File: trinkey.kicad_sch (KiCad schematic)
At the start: 7 parts, among them J1 USB_A, U1 RP2040, U2 AMS1117-3.3

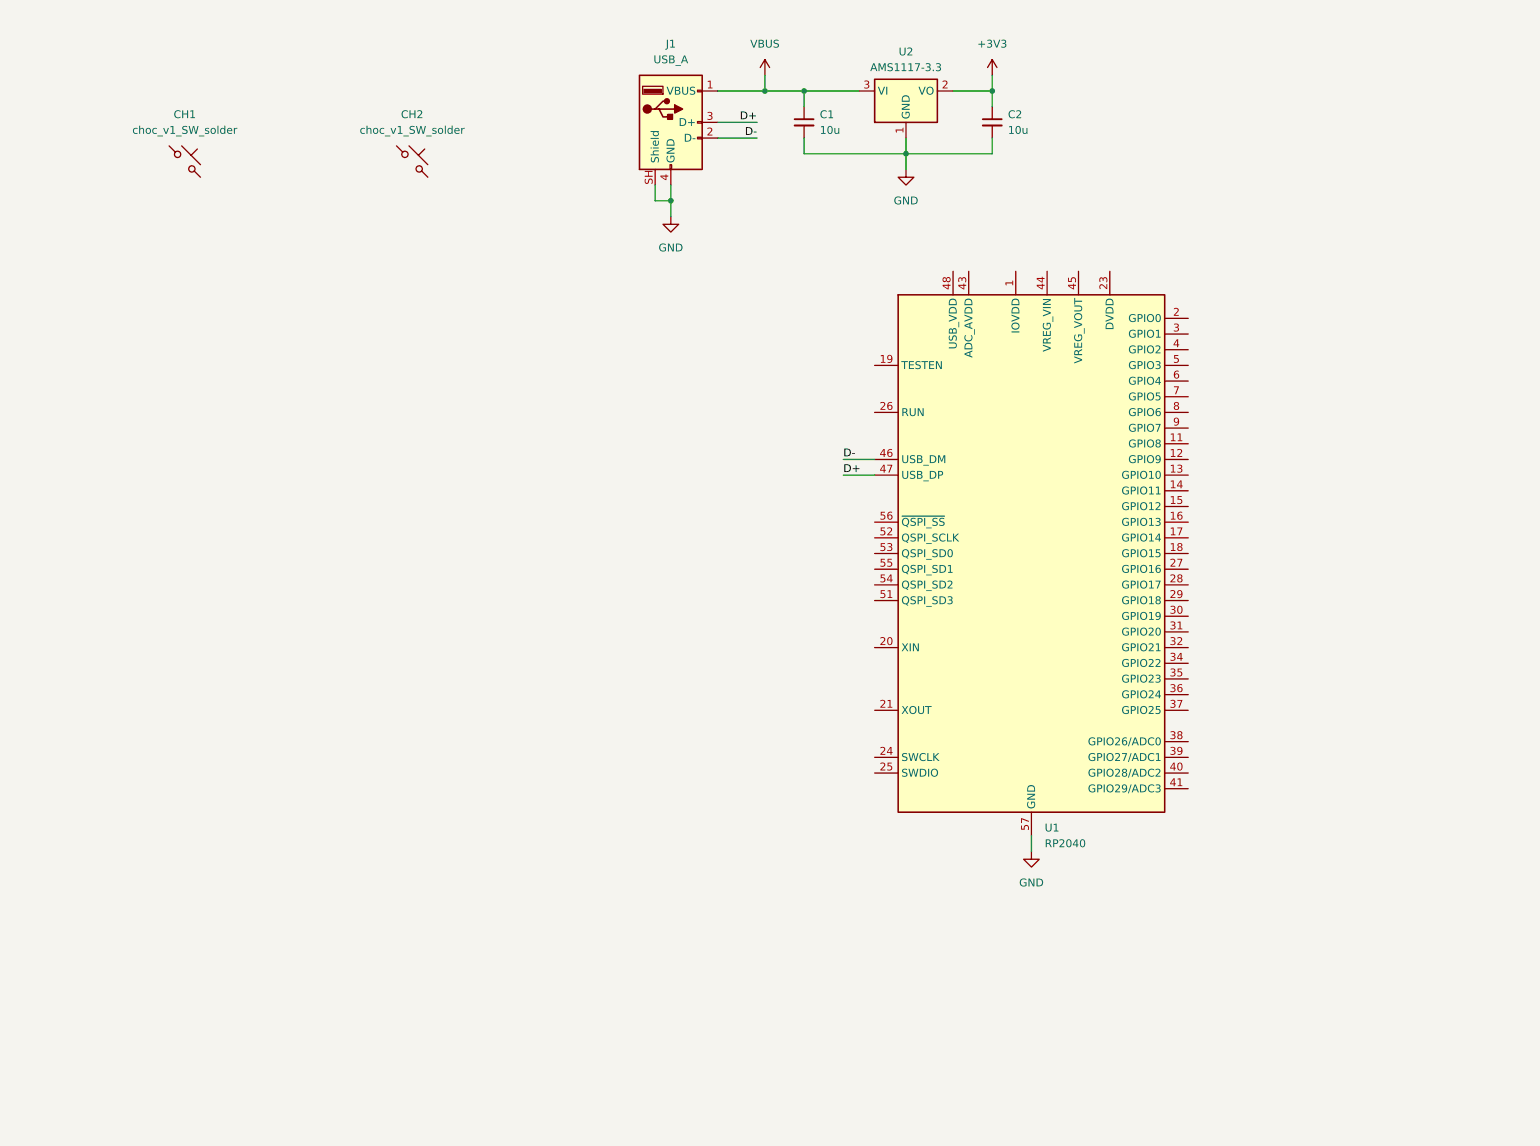
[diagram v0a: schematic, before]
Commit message: feat: basic rp2040 circuitry
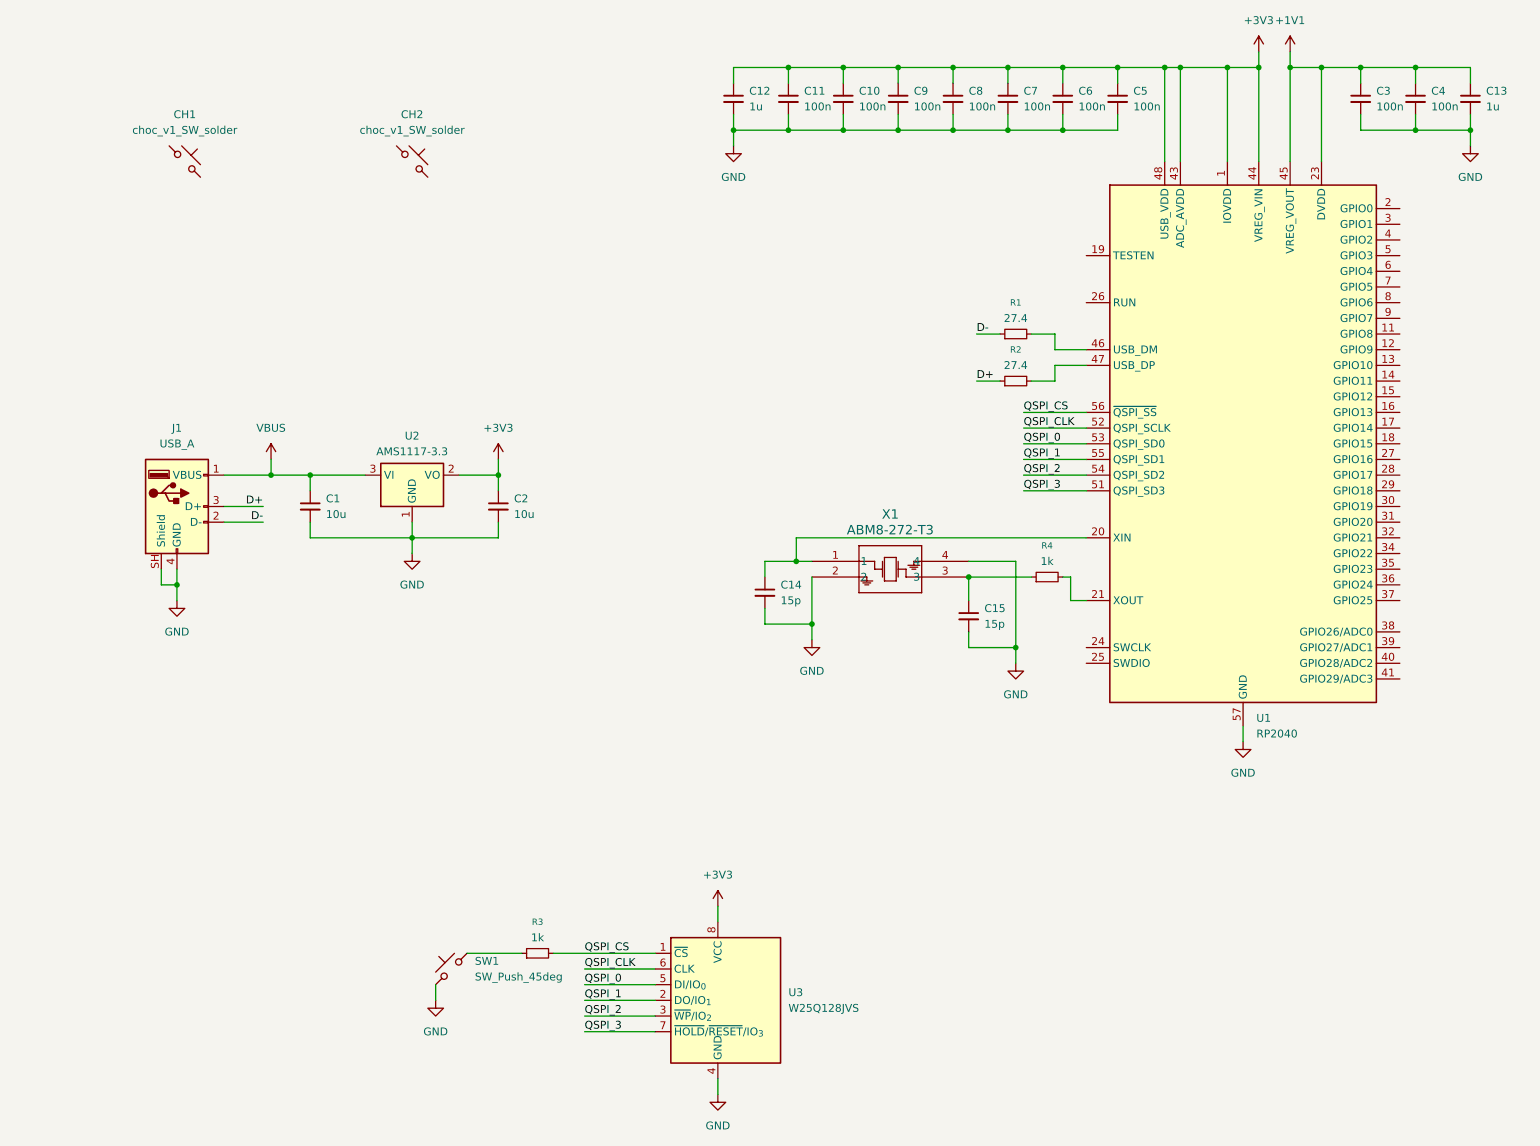
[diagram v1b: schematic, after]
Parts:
- added C10, C11, C3, C4, C5, C6, C7, C8, C9: 100n, symbol Device:C_Small
- added C12, C13: 1u, symbol Device:C_Small
- added C14, C15: 15p, symbol Device:C_Small
- added R1, R2: 27.4, symbol Device:R_Small
- added R3, R4: 1k, symbol Device:R_Small
- added SW1: SW_Push_45deg, symbol Switch:SW_Push_45deg
- added U3: W25Q128JVS, Package_SO:SOIC-8_5.3x5.3mm_P1.27mm, symbol Memory_Flash:W25Q128JVS
- added X1: ABM8-272-T3, ABM8-272-T3:ABM8-272-T3_ABR, symbol ABM8-272-T3:ABM8-272-T3
- U1: footprint Package_DFN_QFN:QFN-56-1EP_7x7mm_P0.4mm_EP3.2x3.2mm_ThermalVias -> Package_DFN_QFN:QFN-56-1EP_7x7mm_P0.4mm_EP3.2x3.2mm
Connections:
- net +3V3: now also U1.1 (IOVDD), U1.10 (IOVDD), U1.22 (IOVDD), U1.33 (IOVDD), U1.42 (IOVDD), U1.43 (ADC_AVDD), U1.44 (VREG_VIN), U1.48 (USB_VDD), U1.49 (IOVDD), C10.1, C11.1, C12.1, C5.1, C6.1, C7.1, C8.1, C9.1, U3.8 (VCC)
- net D+: now also R2.1; no longer U1.47 (USB_DP)
- net D-: now also R1.1; no longer U1.46 (USB_DM)
- net GND: now also C10.2, C11.2, C12.2, C13.2, C14.2, C15.2, C3.2, C4.2, C5.2, C6.2, C7.2, C8.2, C9.2, SW1.1, U3.4 (GND), X1.2, X1.4
- net at U1.20 (XIN): now also C14.1, X1.1
- net at U1.21 (XOUT): now also R4.2
- net +1V1: now reaches U1.23 (DVDD), U1.50 (DVDD)
- net +1V1: now also U1.45 (VREG_VOUT), C13.1, C3.1, C4.1
- net QSPI_3: now reaches U1.51 (QSPI_SD3)
- net QSPI_3: now also U3.7 (~{HOLD}/~{RESET}/IO_{3})
- net QSPI_CLK: now reaches U1.52 (QSPI_SCLK)
- net QSPI_CLK: now also U3.6 (CLK)
- net QSPI_0: now reaches U1.53 (QSPI_SD0)
- net QSPI_0: now also U3.5 (DI/IO_{0})
- net QSPI_2: now reaches U1.54 (QSPI_SD2)
- net QSPI_2: now also U3.3 (~{WP}/IO_{2})
- net QSPI_1: now reaches U1.55 (QSPI_SD1)
- net QSPI_1: now also U3.2 (DO/IO_{1})
- net QSPI_CS: now reaches U1.56 (~{QSPI_SS})
- net QSPI_CS: now also R3.2, U3.1 (~{CS})
- new net: R2.2, U1.47 (USB_DP)
- new net: R1.2, U1.46 (USB_DM)
- new net: R3.1, SW1.2
- new net: C15.1, R4.1, X1.3
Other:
- moved on the sheet: C1, C2, J1, U2

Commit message: feat: packaging ahhhhh
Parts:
- added LED1, LED2: choc_SK6812MINI-E, PCM_marbastlib-choc:LED_choc_6028R, symbol PCM_marbastlib-choc:choc_SK6812MINI-E
- C1, C10, C11, C12, C13, C14, C15, C2, C3, C4, C5, C6, C7, C8, C9: footprint (none) -> Capacitor_SMD:C_0402_1005Metric
- R1, R2, R3, R4: footprint (none) -> Resistor_SMD:R_0402_1005Metric
- SW1: footprint (none) -> TS-1088-AR02016:SW_TS-1088_XNP-L
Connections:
- net +3V3: now also LED1.1 (VDD), LED2.1 (VDD)
- net GND: now also CH1.2, CH2.2, LED1.4 (VSS), LED2.4 (VSS)
- new net: LED1.2 (DOUT), LED2.3 (DIN)
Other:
- moved on the sheet: C1, C2, CH1, J1, U2

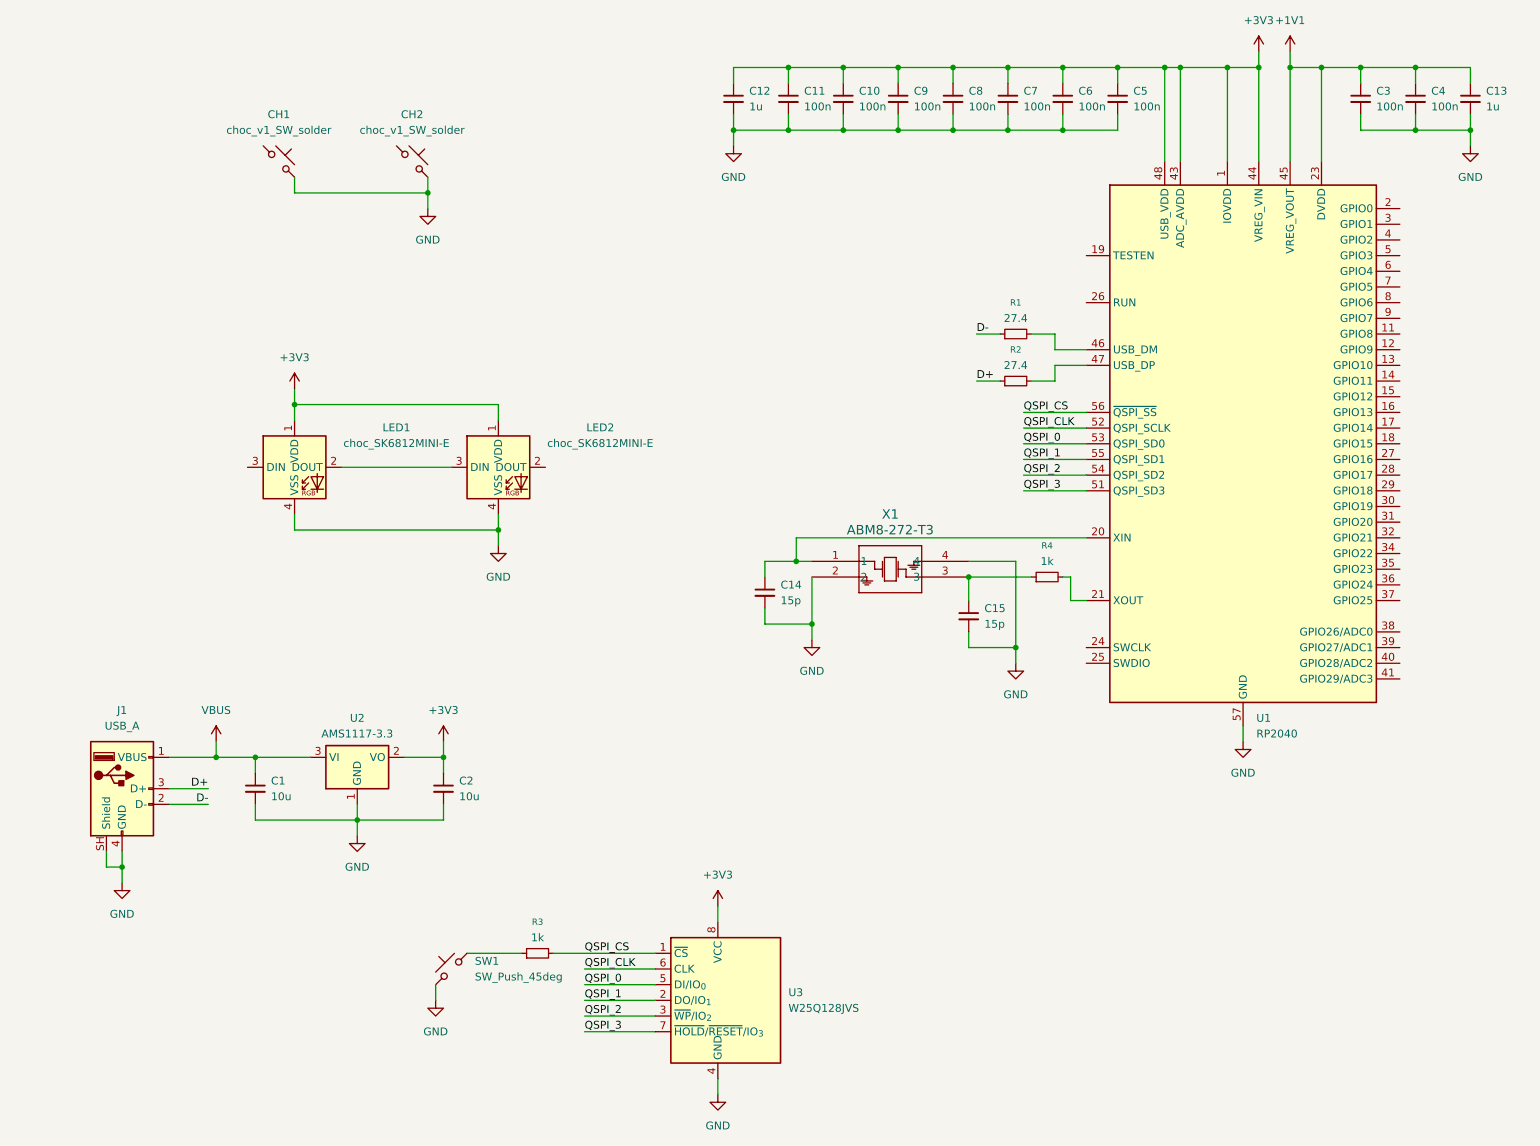
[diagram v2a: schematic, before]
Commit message: feat: switch to the STM32
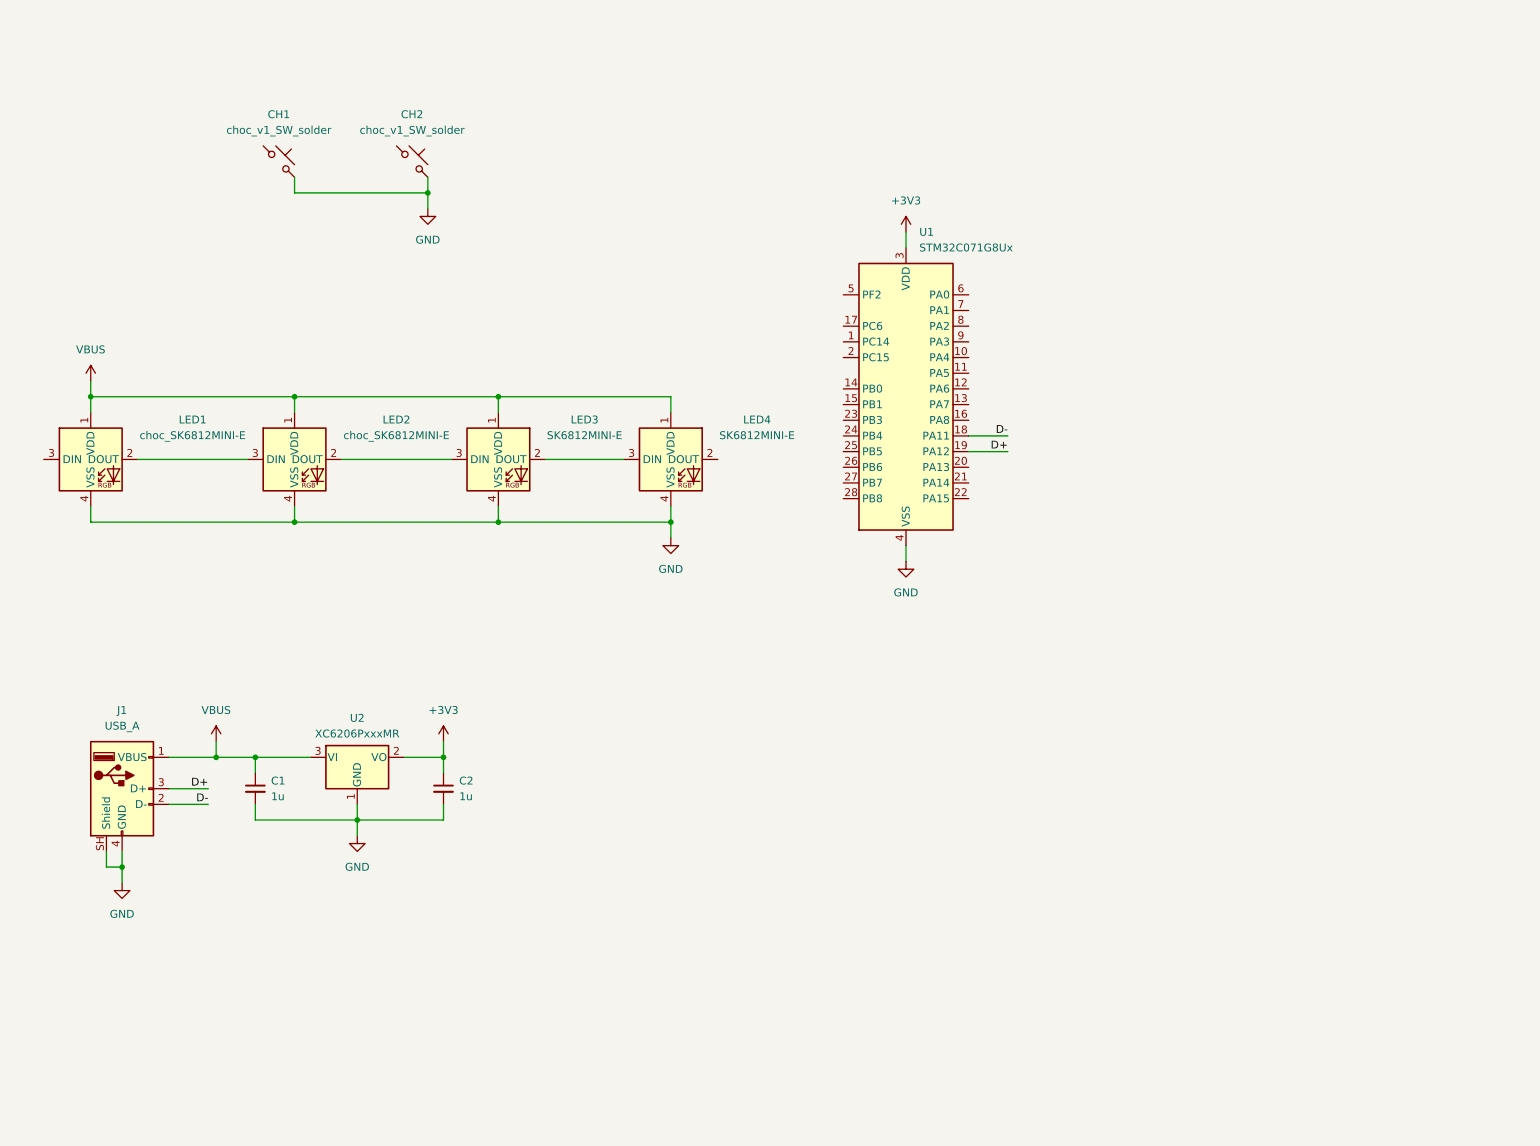
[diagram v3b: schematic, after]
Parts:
- removed C10, C11, C3, C4, C5, C6, C7, C8, C9: 100n, Capacitor_SMD:C_0402_1005Metric, symbol Device:C_Small
- removed C12, C13: 1u, Capacitor_SMD:C_0402_1005Metric, symbol Device:C_Small
- removed C14, C15: 15p, Capacitor_SMD:C_0402_1005Metric, symbol Device:C_Small
- removed R1, R2: 27.4, Resistor_SMD:R_0402_1005Metric, symbol Device:R_Small
- removed R3, R4: 1k, Resistor_SMD:R_0402_1005Metric, symbol Device:R_Small
- removed SW1: SW_Push_45deg, TS-1088-AR02016:SW_TS-1088_XNP-L, symbol Switch:SW_Push_45deg
- removed U1: RP2040, Package_DFN_QFN:QFN-56-1EP_7x7mm_P0.4mm_EP3.2x3.2mm, symbol MCU_RaspberryPi:RP2040
- removed U2: AMS1117-3.3, Package_TO_SOT_SMD:SOT-223-3_TabPin2, symbol Regulator_Linear:AMS1117-3.3
- removed U3: W25Q128JVS, Package_SO:SOIC-8_5.3x5.3mm_P1.27mm, symbol Memory_Flash:W25Q128JVS
- removed X1: ABM8-272-T3, ABM8-272-T3:ABM8-272-T3_ABR, symbol ABM8-272-T3:ABM8-272-T3
- added LED3, LED4: SK6812MINI-E, PCM_marbastlib-various:LED_6028R, symbol PCM_marbastlib-various:SK6812MINI-E
- added U1: STM32C071G8Ux, Package_DFN_QFN:QFN-28_4x4mm_P0.5mm, symbol MCU_ST_STM32C0:STM32C071G8Ux
- added U2: XC6206PxxxMR, Package_TO_SOT_SMD:SOT-23-3, symbol Regulator_Linear:XC6206PxxxMR
- C1, C2: value 10u -> 1u
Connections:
- net +3V3: now also U1.3 (VDD), U2.2 (VO); no longer LED1.1 (VDD), LED2.1 (VDD)
- net D+: now also U1.19 (PA12)
- net D-: now also U1.18 (PA11)
- net GND: now also LED3.4 (VSS), LED4.4 (VSS), U1.4 (VSS), U2.1 (GND)
- net VBUS: now also LED1.1 (VDD), LED2.1 (VDD), LED3.1 (VDD), LED4.1 (VDD), U2.3 (VI)
- net at LED2.2 (DOUT): now also LED3.3 (DIN)
- new net: LED3.2 (DOUT), LED4.3 (DIN)
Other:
- moved on the sheet: LED1, LED2

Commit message: feat: polishing and readme
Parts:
- added C3, C6, C7, C8, C9: 100n, Capacitor_SMD:C_0402_1005Metric, symbol Device:C_Small
- added C4: 4.7u, Capacitor_SMD:C_0402_1005Metric, symbol Device:C_Small
- added C5: 10u, Capacitor_SMD:C_0402_1005Metric, symbol Device:C_Small
- added R1: 47, Resistor_SMD:R_0402_1005Metric, symbol Device:R_Small
- added TP1: SWDIO, TestPoint:TestPoint_Pad_D1.0mm, symbol Connector:TestPoint_Probe
- added TP2: SWCLK, TestPoint:TestPoint_Pad_D1.0mm, symbol Connector:TestPoint_Probe
- added TP3: NRST, TestPoint:TestPoint_Pad_D1.0mm, symbol Connector:TestPoint_Probe
- added TP4: 3V3, TestPoint:TestPoint_Pad_D1.0mm, symbol Connector:TestPoint_Probe
- added TP5: GND, TestPoint:TestPoint_Pad_D1.0mm, symbol Connector:TestPoint_Probe
- added U3: USBLC6-2SC6, Package_TO_SOT_SMD:SOT-23-6, symbol Power_Protection:USBLC6-2SC6
- added U4: 74AHCT1G125, Package_TO_SOT_SMD:SOT-23-5, symbol 74xGxx:74AHCT1G125
- C1, C2: LCSC Part # (none) -> C52923
- U1: LCSC Part # (none) -> C44521811
- U2: LCSC Part # (none) -> C347376
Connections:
- net +3V3: now also C3.1, C4.1, TP4.1
- net D+: now also U3.4 (I/O2); no longer J1.3 (D+)
- net D-: now also U3.6 (I/O1); no longer J1.2 (D-)
- net GND: now also CH1.1, CH2.1, C3.2, C4.2, C5.2, C6.2, C7.2, C8.2, C9.2, TP5.1, U3.2 (GND), U4.1, U4.3 (GND); no longer CH1.2, CH2.2
- net VBUS: now also C5.1, C6.1, C7.1, C8.1, C9.1, U3.5 (VBUS), U4.5 (VCC)
- net SW2: now reaches U1.1 (PC14)
- net SW2: now also CH2.2
- net SW1: now reaches U1.20 (PA13)
- net SW1: now also CH1.2, TP1.1
- net SWCLK: now reaches U1.21 (PA14)
- net SWCLK: now also TP2.1
- net LED_DATA: now reaches U1.24 (PB4)
- net LED_DATA: now also U4.2
- net NRST: now reaches U1.5 (PF2)
- net NRST: now also TP3.1
- net at LED1.3 (DIN): now also R1.2
- new net: J1.2 (D-), U3.1 (I/O1)
- new net: J1.3 (D+), U3.3 (I/O2)
- new net: R1.1, U4.4
- no-connect marks 0 -> 20
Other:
- moved on the sheet: C1, C2, LED1, LED2, LED3, LED4, U1, U2
